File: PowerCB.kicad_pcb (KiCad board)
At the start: 2 copper layers, 54 x 15.1 mm, 16 parts, among them J1 USB_B_Micro, J2 Mounting_1, J3 Mounting_2, J6 Conn_01x02_Male, J7 Conn_01x02_Male, J8 Conn_01x02_Male, J9 Conn_01x02_Male, U1 TPS73633DBV

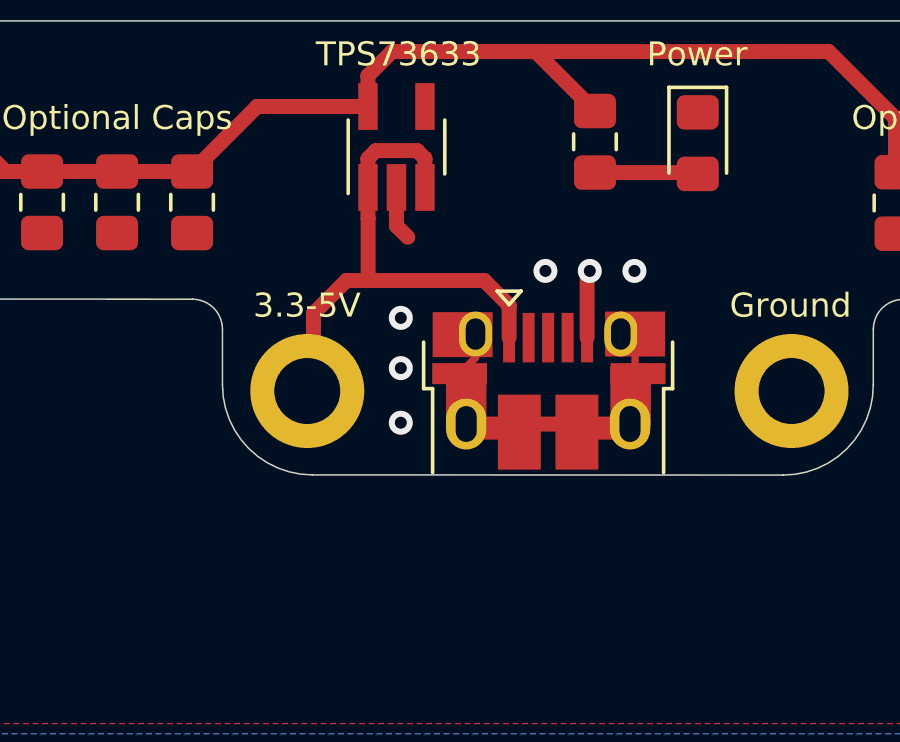
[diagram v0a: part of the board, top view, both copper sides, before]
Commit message: feat: USB-C instead of Micro-USB connector
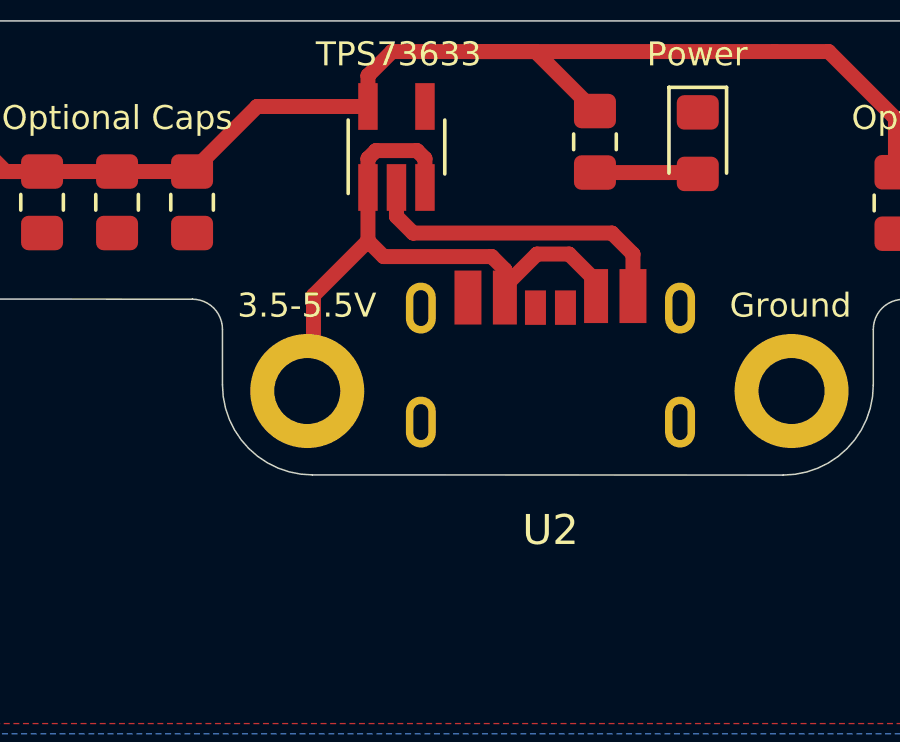
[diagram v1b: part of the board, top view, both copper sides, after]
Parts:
- removed J1: USB_B_Micro, Connector_USB:USB_Micro-B_Amphenol_10103594-0001LF_Horizontal
- added U2: USB-C-Power, PowerCB:UJC-HP-3-SMT-TR, F.Cu at (38.8, 20.9)
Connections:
- net Net-(J1-Pad1) renamed +5V
- U1 pad 4: (no net) -> Net-(U1-Pad4)
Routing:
- net Net-(J1-Pad6): track 13.9 -> 0.00 mm
- net GND: track 3.86 -> 10.8 mm, vias 11 -> 5
- net +5V: track 18.2 -> 22.4 mm
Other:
- board text added: "3.5-5.5V"
- board text added: "V 02"
- board text removed: "3.3-5V"
- board text removed: "V 01"

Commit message: chore: convert to KiCad 6 file formats
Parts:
- U2: footprint PowerCB:UJC-HP-3-SMT-TR -> USB-C:UJC-HP-3-SMT-TR
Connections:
- U1 pad 4: Net-(U1-Pad4) -> unconnected-(U1-Pad4)
- U2 pad 3: Net-(U2-Pad3) -> unconnected-(U2-Pad3)
- U2 pad 4: Net-(U2-Pad4) -> unconnected-(U2-Pad4)
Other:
- net class Default removed

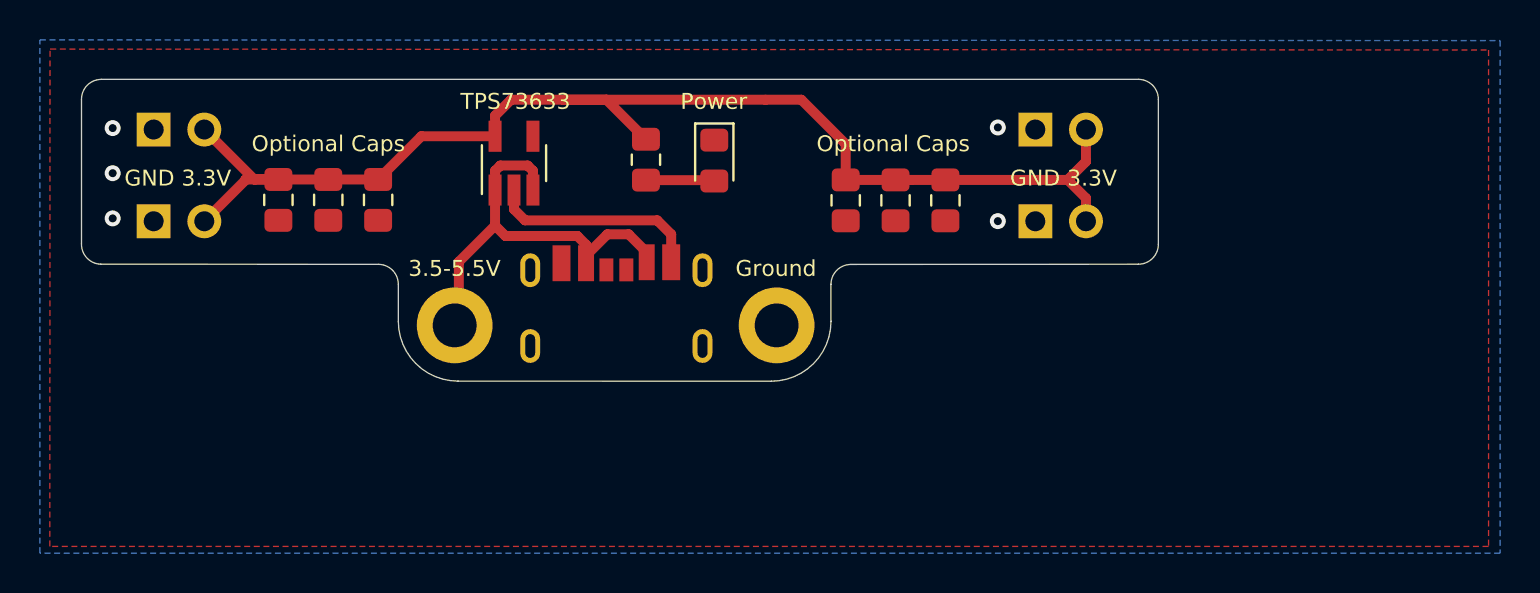
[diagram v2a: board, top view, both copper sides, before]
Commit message: feat: M3 instead of M2 mounting holes
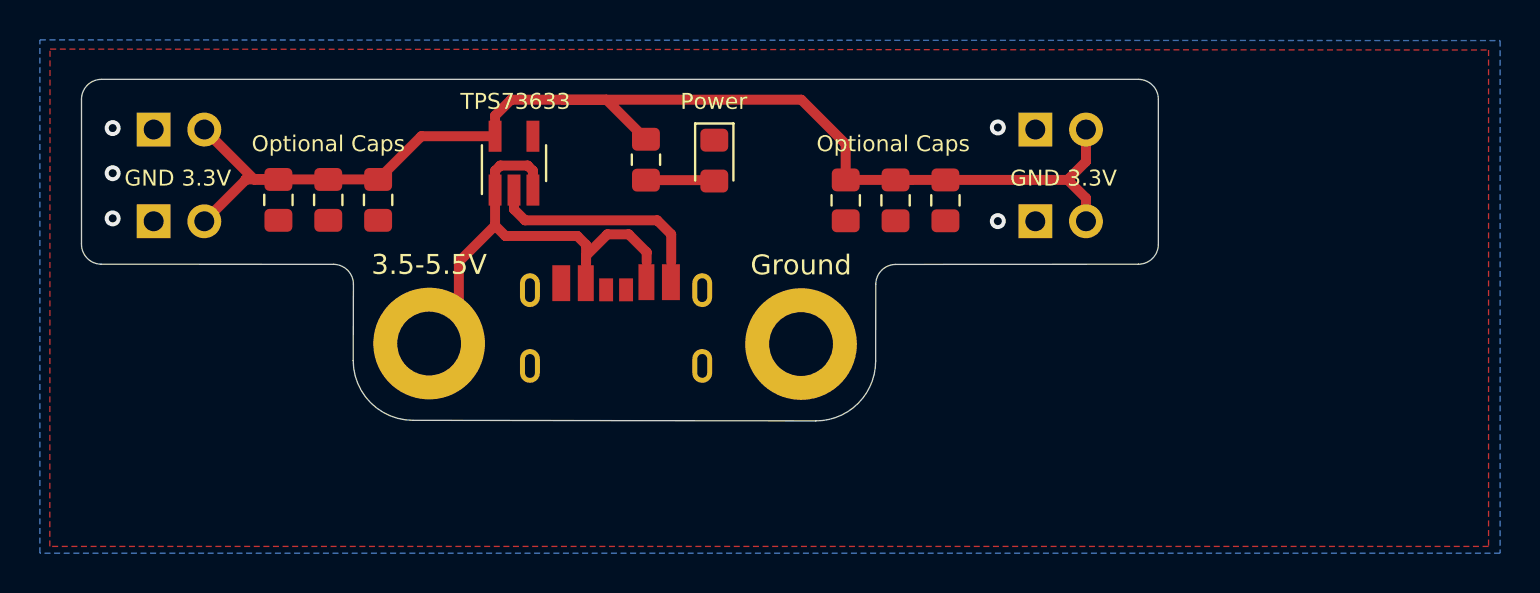
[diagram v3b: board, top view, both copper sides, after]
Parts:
- removed J2: Mounting_1, MountingHole:MountingHole_2.2mm_M2_DIN965_Pad
- removed J3: Mounting_2, MountingHole:MountingHole_2.2mm_M2_DIN965_Pad
- added H1: 3.5-5.5V, MountingHole:MountingHole_3.2mm_M3_DIN965_Pad, F.Cu at (29.4, 25.2)
- added H2: Ground, MountingHole:MountingHole_3.2mm_M3_DIN965_Pad, F.Cu at (48.1, 25.2)
- moved U2 1.00 mm to (38.8, 21.9)
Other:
- board size 54 x 15.1 mm -> 54 x 17.1 mm
- board text added: "V 03"
- board text removed: "3.5-5.5V"
- board text removed: "Ground"
- board text removed: "V 02"

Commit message: fix: missing USB-C CC pulldown resistors
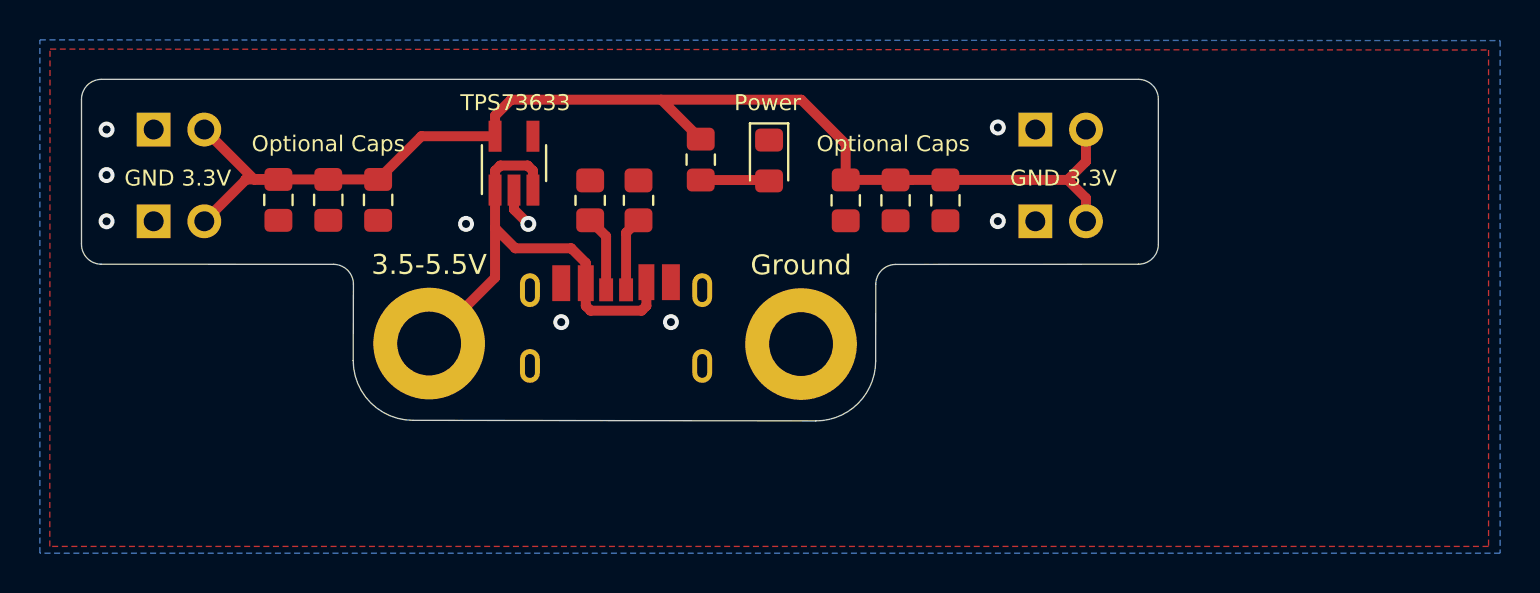
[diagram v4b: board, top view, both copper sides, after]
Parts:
- added R2: 5.1k, Resistor_SMD:R_0805_2012Metric_Pad1.20x1.40mm_HandSolder, F.Cu at (37.5, 18.0)
- added R3: 5.1k, Resistor_SMD:R_0805_2012Metric_Pad1.20x1.40mm_HandSolder, F.Cu at (40.0, 18.0)
- moved D1 2.75 mm to (46.5, 16.0)
- moved R1 2.75 mm to (43.1, 16.0)
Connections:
- U2 pad 3: unconnected-(U2-Pad3) -> Net-(U2-Pad3)
- U2 pad 4: unconnected-(U2-Pad4) -> Net-(U2-Pad4)
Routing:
- net GND: track 10.8 -> 1.99 mm, vias 5 -> 9
- net Net-(U2-Pad3): track 0.00 -> 3.82 mm
- net Net-(U2-Pad4): track 0.00 -> 3.75 mm
- net +5V: track 22.3 -> 25.0 mm
- net +3V3: track 64.3 -> 62.2 mm

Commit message: feat: OSHW logo
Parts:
- added REF**: OSHW-Logo2_7.3x6mm_SilkScreen, Symbol:OSHW-Logo2_7.3x6mm_SilkScreen, B.Cu at (26.1, 16.7)
